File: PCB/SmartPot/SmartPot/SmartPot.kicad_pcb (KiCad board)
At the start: 2 copper layers, 86.8 x 42.6 mm, 51 parts, among them J1 Screw_Terminal_01x02, J2 Screw_Terminal_01x02, J3 Conn_01x03_Pin, J4 Barrel_Jack_MountingPin, J5 Conn_01x03_Pin, J6 Conn_01x04_Pin, J7 Conn_01x02_Pin, J8 Conn_01x02_Pin, J9 Screw_Terminal_01x04, K1 AWHSH112DM00G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

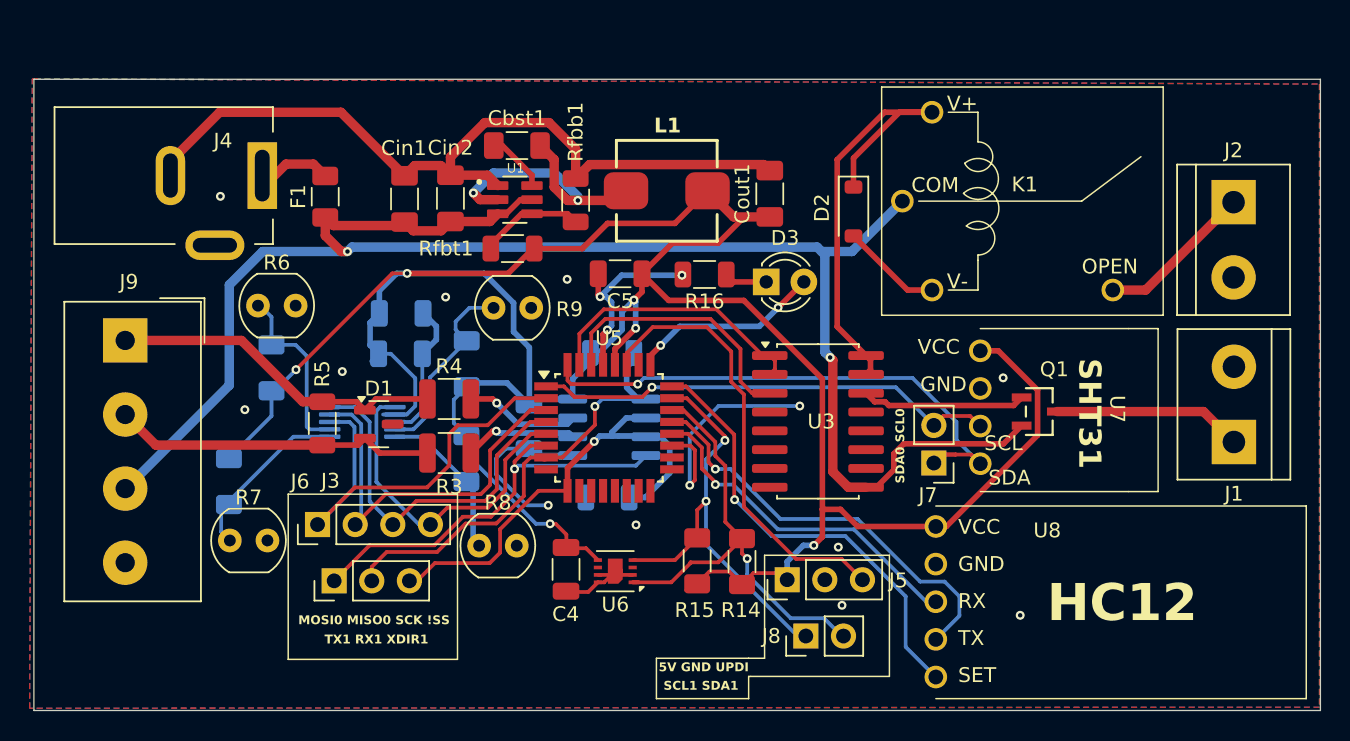
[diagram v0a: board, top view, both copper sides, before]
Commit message: Added code fro rasp zero and updated the PCB
Signed-off-by: Simonca Raul <simonca.raul@gmail.com>
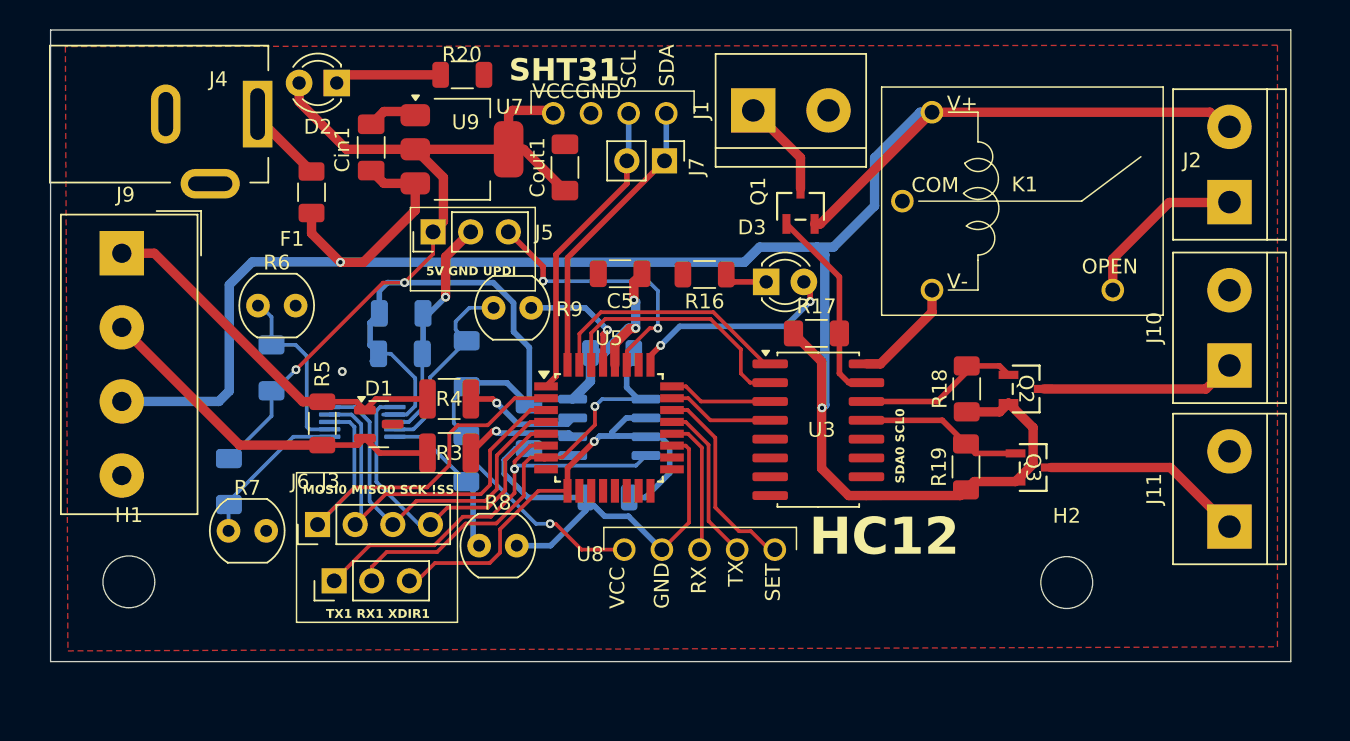
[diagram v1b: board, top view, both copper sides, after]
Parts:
- removed C4: 100nF, Capacitor_SMD:C_1206_3216Metric
- removed Cbst1: 100nF, Capacitor_SMD:C_1206_3216Metric_Pad1.33x1.80mm_HandSolder
- removed Cin2: 10uF, Capacitor_SMD:C_1206_3216Metric_Pad1.33x1.80mm_HandSolder
- removed J8: Conn_01x02_Pin, Connector_PinHeader_2.54mm:PinHeader_1x02_P2.54mm_Vertical
- removed L1: 4.7uH, Inductor_SMD:L_6.8x6.8_H3
- removed R14, R15: 20kOhm, Resistor_SMD:R_1206_3216Metric_Pad1.30x1.75mm_HandSolder
- removed Rfbb1: 10kOhm, Resistor_SMD:R_1206_3216Metric
- removed Rfbt1: 56.2kOhm, Resistor_SMD:R_1206_3216Metric
- removed U1: TPS561208DDCT, Converter_DCDC:SOT95P280X110-6N
- removed U6: SHT31A-DIS, Sensor_Humidity:Sensirion_DFN-8-1EP_2.5x2.5mm_P0.5mm_EP1.1x1.7mm
- added H1: MountingHole, MountingHole:MountingHole_3.5mm, F.Cu at (174.1, 117.3)
- added H2: MountingHole, MountingHole:MountingHole_3.5mm, F.Cu at (237.4, 117.4)
- added J10: Screw_Terminal_01x02, TerminalBlock:TerminalBlock_bornier-2_P5.08mm, F.Cu at (248.4, 102.7)
- added J11: Screw_Terminal_01x02, TerminalBlock:TerminalBlock_bornier-2_P5.08mm, F.Cu at (248.4, 113.6)
- added Q2: SSM3J352F_LF, Package_S-Mini:S-MINI_TOS, F.Cu at (234.7, 104.3)
- added Q3: SSM3J352F_LF, Package_S-Mini:S-MINI_TOS, F.Cu at (235.2, 109.6)
- added R17: 10kohm, Resistor_SMD:R_1206_3216Metric_Pad1.30x1.75mm_HandSolder, F.Cu at (220.6, 100.6)
- added R18: 10kohm, Resistor_SMD:R_1206_3216Metric_Pad1.30x1.75mm_HandSolder, F.Cu at (230.7, 104.3)
- added R19: 10kohm, Resistor_SMD:R_1206_3216Metric_Pad1.30x1.75mm_HandSolder, F.Cu at (230.6, 109.6)
- added R20: 250-400 Ohm, Resistor_SMD:R_1206_3216Metric, F.Cu at (196.7, 83.1)
- added U9: LT1117-5.0, Package_TO_SOT_SMD:SOT-223-3_TabPin2, F.Cu at (196.6, 88.2)
- Cin1: value 10uF -> 100nF
- Cout1: value 47uF -> 10uF
- D2: value 1N4148W -> LED; footprint Diode_SMD:D_SOD-123 -> LED_THT:LED_D3.0mm_FlatTop
- moved J1 39.4 mm to (216.3, 85.5), turned to 0 degrees
- moved D2 35.9 mm to (188.2, 83.7), turned to 180 degrees
- moved J5 33.5 mm to (194.7, 93.7)
- moved U7 33.0 mm to (202.8, 85.7), turned to 0 degrees
- moved J7 27.3 mm to (210.3, 88.9), turned to -90 degrees
- moved Q1 21.2 mm to (219.5, 92.0), turned to 0 degrees
- moved U8 21.0 mm to (207.7, 115.2), turned to 0 degrees
- moved Cout1 13.9 mm to (203.6, 89.4)
- moved J9 5.89 mm to (173.7, 95.2)
- moved J4 4.16 mm to (182.8, 85.8)
- moved Cin1 4.14 mm to (190.5, 88.0)
- moved F1 0.97 mm to (186.5, 91.0)
- moved R7 0.66 mm to (180.9, 113.9)
- moved U3 0.56 mm to (220.7, 107.1)
- moved J2 0.28 mm to (248.4, 91.7), turned to 90 degrees
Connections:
- net /LOAD renamed /LOAD1
- net /MOSI0 renamed /DIN
- net Net-(F1-Pad2) renamed /12Out
- D2 pad 1: /OUT1 -> Net-(D2-K)
- D2 pad 2: GND -> +5V
- J2 pad 2: GND -> +12V
- K1 pad COM: +12V -> GND
- K1 pad V+: /OUT1 -> +12V
- K1 pad V-: GND -> /OUT1
- U3 pad 13: unconnected-(U3-O4-Pad13) -> /OUT4
- U3 pad 14: /OUT2 -> /OUT3
- U3 pad 15: /OUT1 -> /OUT2
- U3 pad 2: /COMM1 -> /COMM2
- U3 pad 3: /COMM2 -> /COMM3
- U3 pad 4: unconnected-(U3-I4-Pad4) -> /COMM4
- U5 pad 22: /SDA1 -> /SET
- U5 pad 23: /SCL1 -> /COMM4
- U5 pad 24: /SET -> /COMM3
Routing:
- net +5V: track 191.0 -> 128.0 mm, vias 6 -> 5
- net GND: track 117.8 -> 61.6 mm, vias 16 -> 3
- net +12V: track 114.0 -> 160.8 mm
- net /SDA1: track 30.8 -> 0.00 mm, vias 1 -> 0
- net /SCL1: track 29.3 -> 0.00 mm, vias 2 -> 0
- net /OUT1: track 31.8 -> 7.37 mm
- net /SW: track 19.0 -> 0.00 mm, vias 2 -> 0
- net /SDA0: track 37.7 -> 19.7 mm, vias 1 -> 0
- net /RX2: track 28.5 -> 11.0 mm, vias 1 -> 0
- net /SET: track 30.5 -> 14.4 mm, vias 1 -> 0
- net /TX2: track 23.7 -> 9.36 mm, vias 1 -> 0
- net /LOAD3: track 0.00 -> 13.7 mm
- net /LOAD2: track 0.00 -> 13.2 mm
- net /OUT3: track 0.00 -> 11.1 mm
- net /OUT4: track 0.00 -> 11.0 mm
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- removed copper zone on B.Cu, net GND
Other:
- board size 86.8 x 42.6 mm -> 83.7 x 42.6 mm
- board text removed: "SCL1 SDA1"
